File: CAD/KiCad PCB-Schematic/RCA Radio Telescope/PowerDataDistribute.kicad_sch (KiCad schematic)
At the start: 31 parts, among them J7 USB_A, J8 USB_A, Q1 DMP4047LFDE-7, U13 MIC23050-SYML-TR, U14 TPS62133RGTR

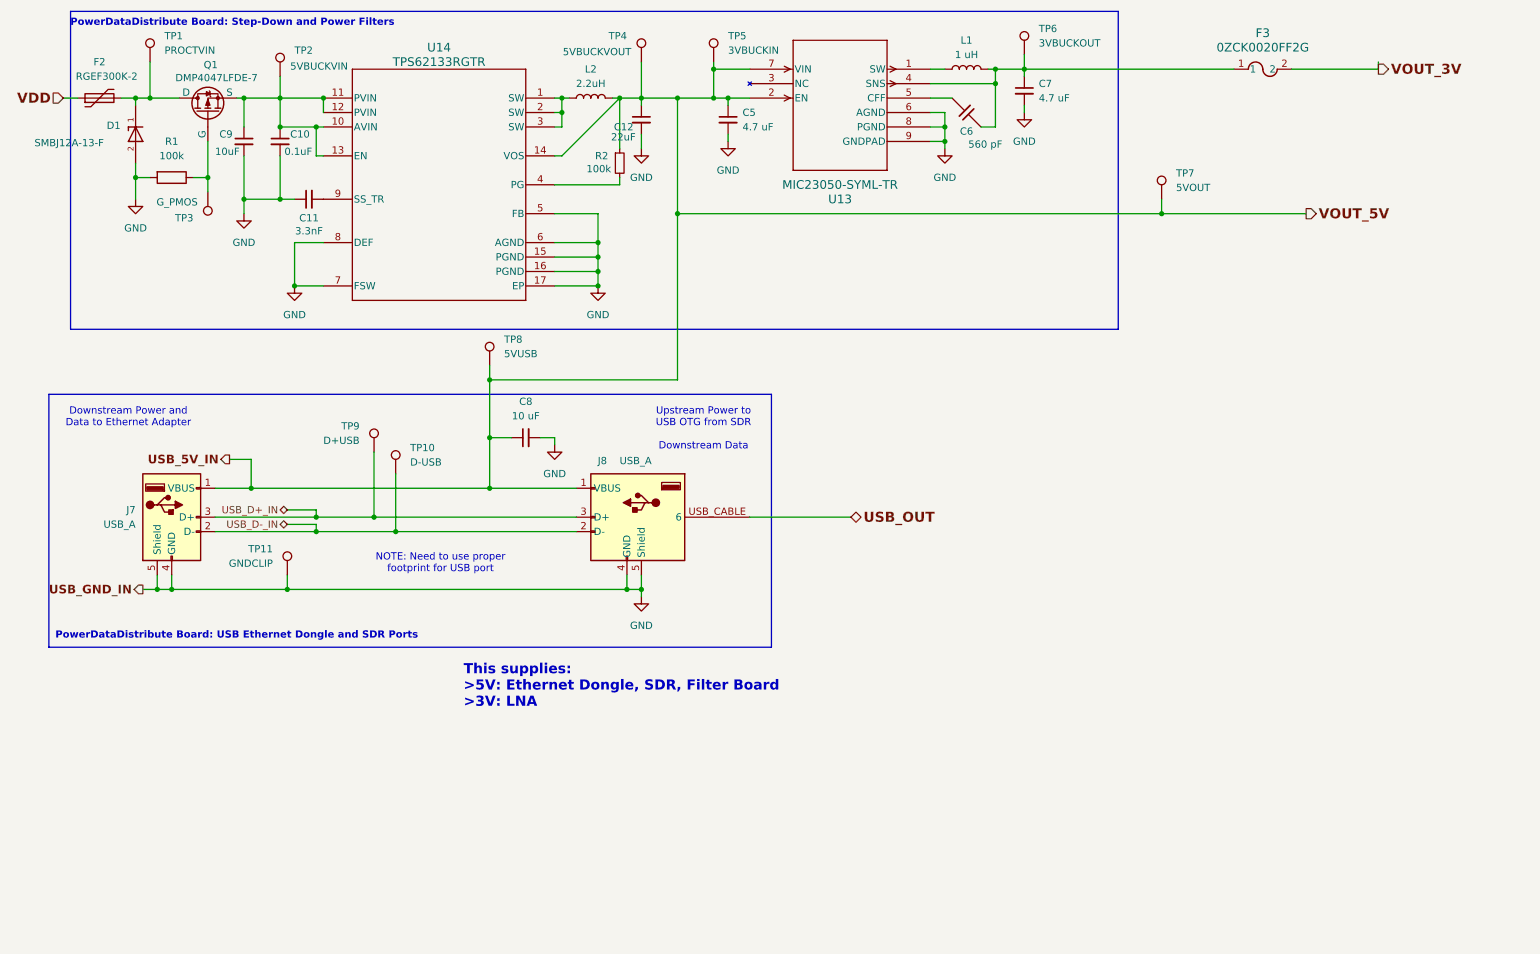
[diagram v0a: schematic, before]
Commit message: Updated PowerData Schematic to v1.8 and PCB to v1.7
- Swapped MIC Buck to LDO
- Changed footprint for Buck Inductor to appropriate component
- Rearranged PCB layout to accommodate new inductor
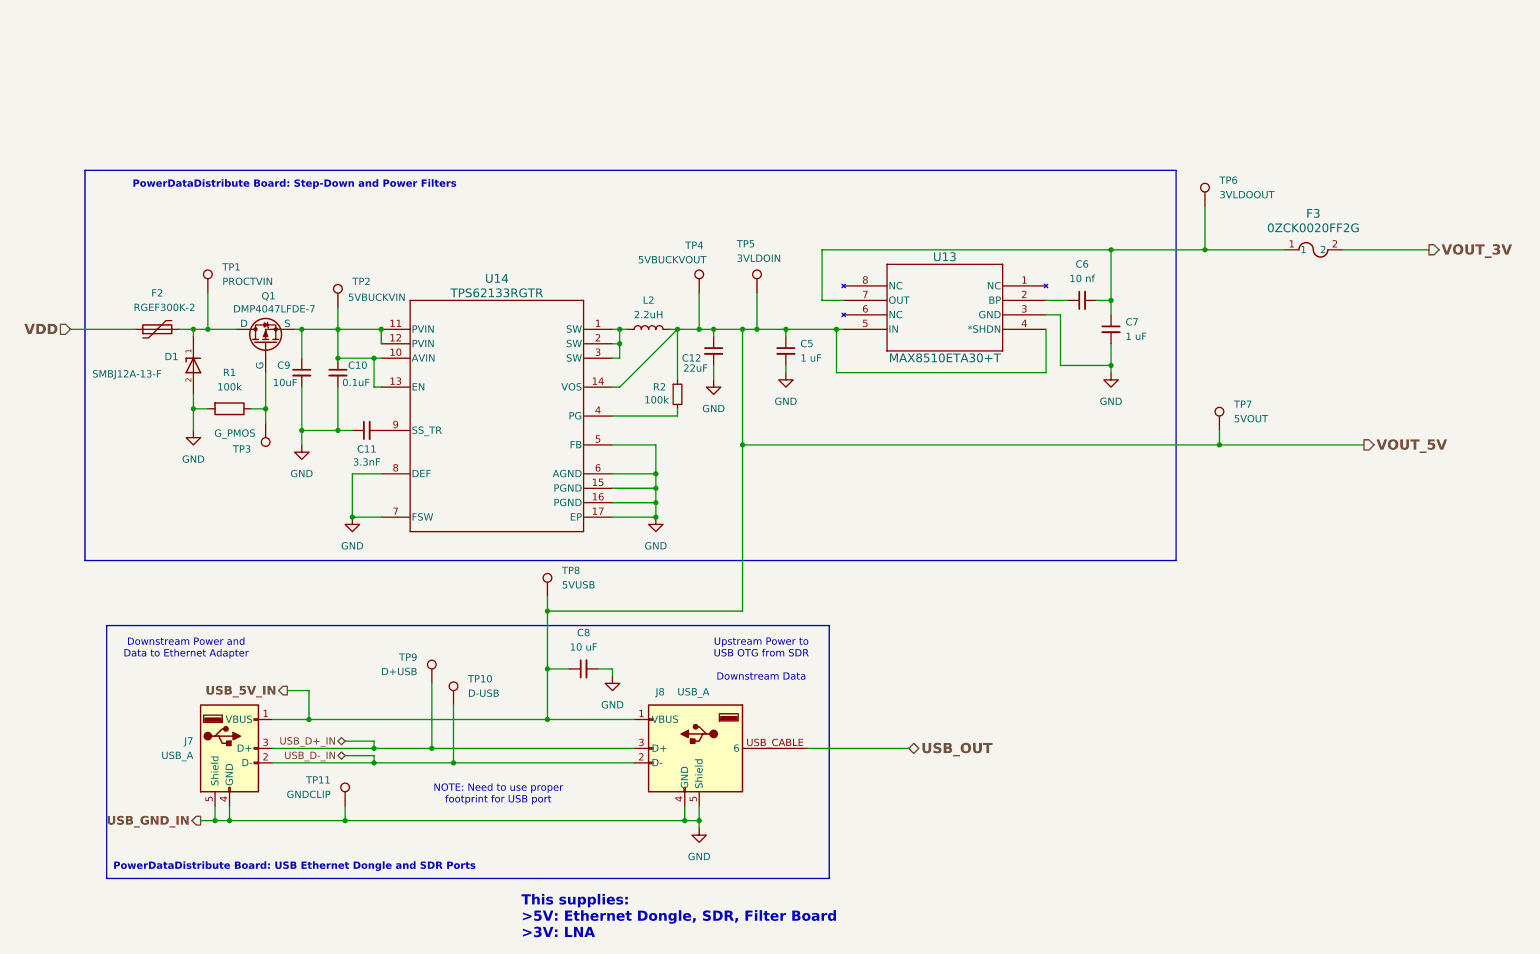
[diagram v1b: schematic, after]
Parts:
- removed C6: 560 pF, Capacitor_SMD:C_0805_2012Metric, symbol Device:C_45deg
- removed L1: 1 uH, Inductor_SMD:L_0805_2012Metric, symbol Device:L
- removed U13: MIC23050-SYML-TR, Library:MLF-8_ML_MCH, symbol Radio Telescope:MIC23050-SYML-TR
- added C6: 10 nf, Capacitor_SMD:C_0805_2012Metric, symbol Device:C_Small
- added U13: MAX8510ETA30+T, Library:21-0168E_T822-1_MXM, symbol Radio Telescope:MAX8510ETA30+T
- C5, C7: value 4.7 uF -> 1 uF
- L2: footprint Inductor_SMD:L_0805_2012Metric -> Library:IND_CB_DRA73
- TP5: value 3VBUCKIN -> 3VLDOIN
- TP6: value 3VBUCKOUT -> 3VLDOOUT
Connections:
- net GND: now also U13.3 (GND)
- net USB_5V_IN: now also U13.4 (*SHDN), U13.5 (IN)
- net at C7.1, F3.1, TP6.1: now also C6.2, U13.7 (OUT)
- new net: C6.1, U13.2 (BP)
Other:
- moved on the sheet: C10, C11, C12, C5, C7, C8, C9, D1, F2, F3, J7, J8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

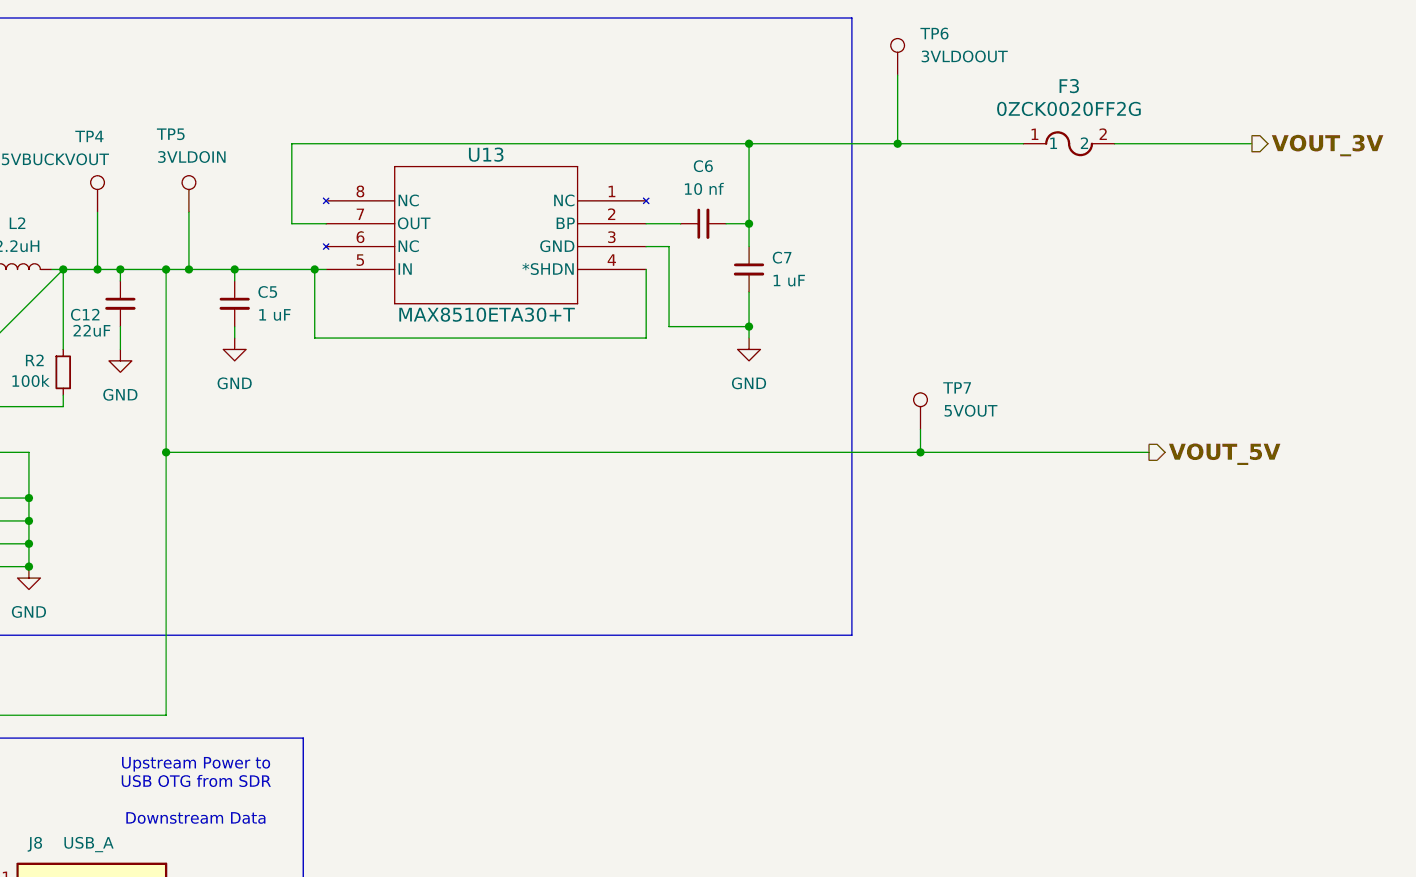
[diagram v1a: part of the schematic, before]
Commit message: Updated PowerData Schematic to v1.9 and PCB to v1.8
- Swapped LDO (Obsolete) with an Active version in both Schematic and PCB
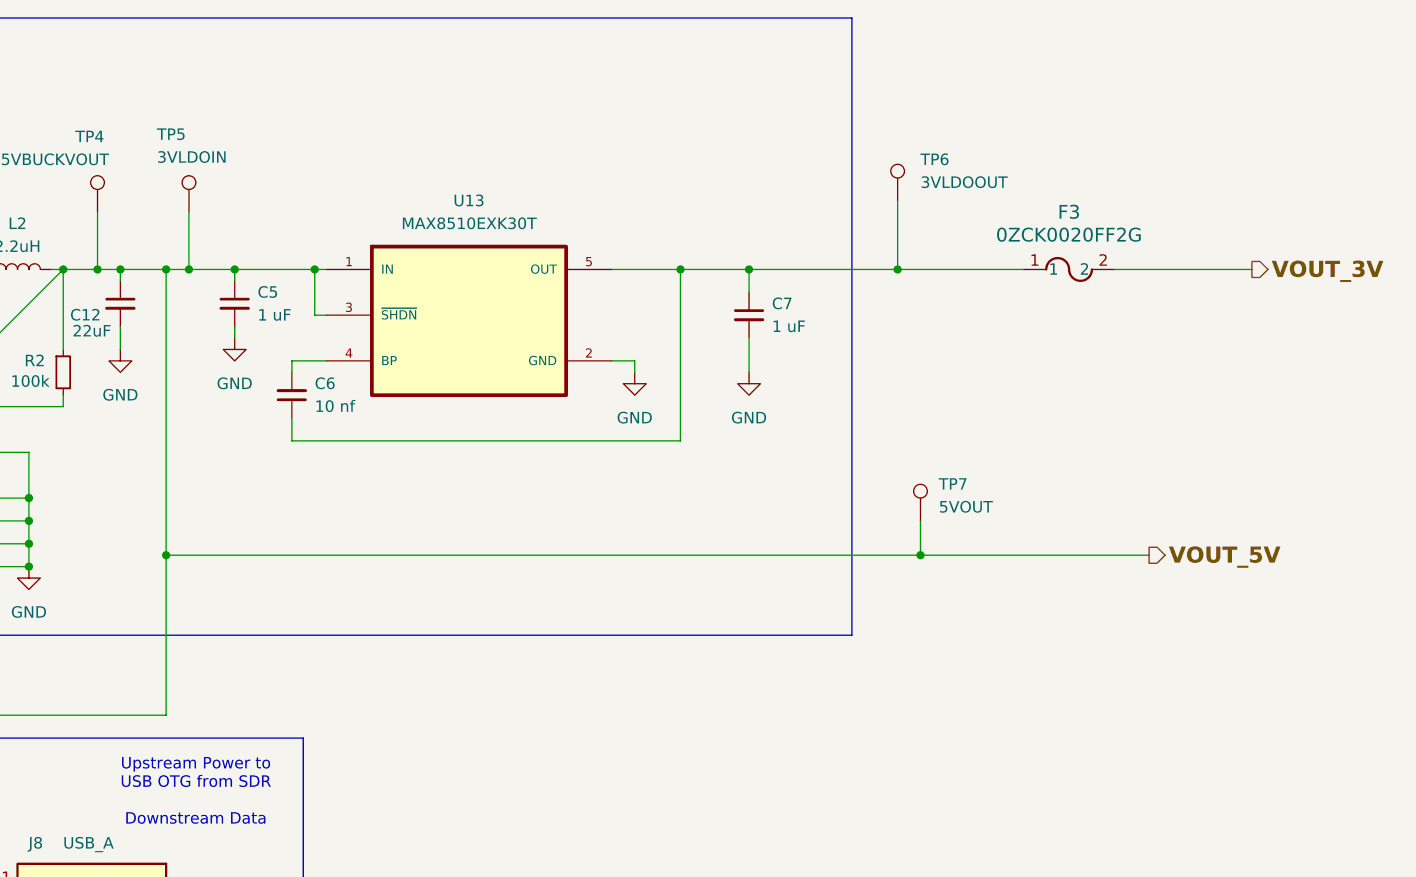
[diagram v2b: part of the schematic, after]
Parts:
- removed U13: MAX8510ETA30+T, Library:21-0168E_T822-1_MXM, symbol Radio Telescope:MAX8510ETA30+T
- added U13: MAX8510EXK30T, Library:SOT65P210X110-5N, symbol Radio Telescope:MAX8510EXK30T
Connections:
- net GND: now also U13.2 (GND)
- net USB_5V_IN: now also U13.1 (IN), U13.3 (~{SHDN})
- net at C6.1: now also C7.1, F3.1, TP6.1, U13.5 (OUT)
- new net: C6.2, U13.4 (BP)
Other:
- moved on the sheet: C6, C7, F3, TP6, TP7

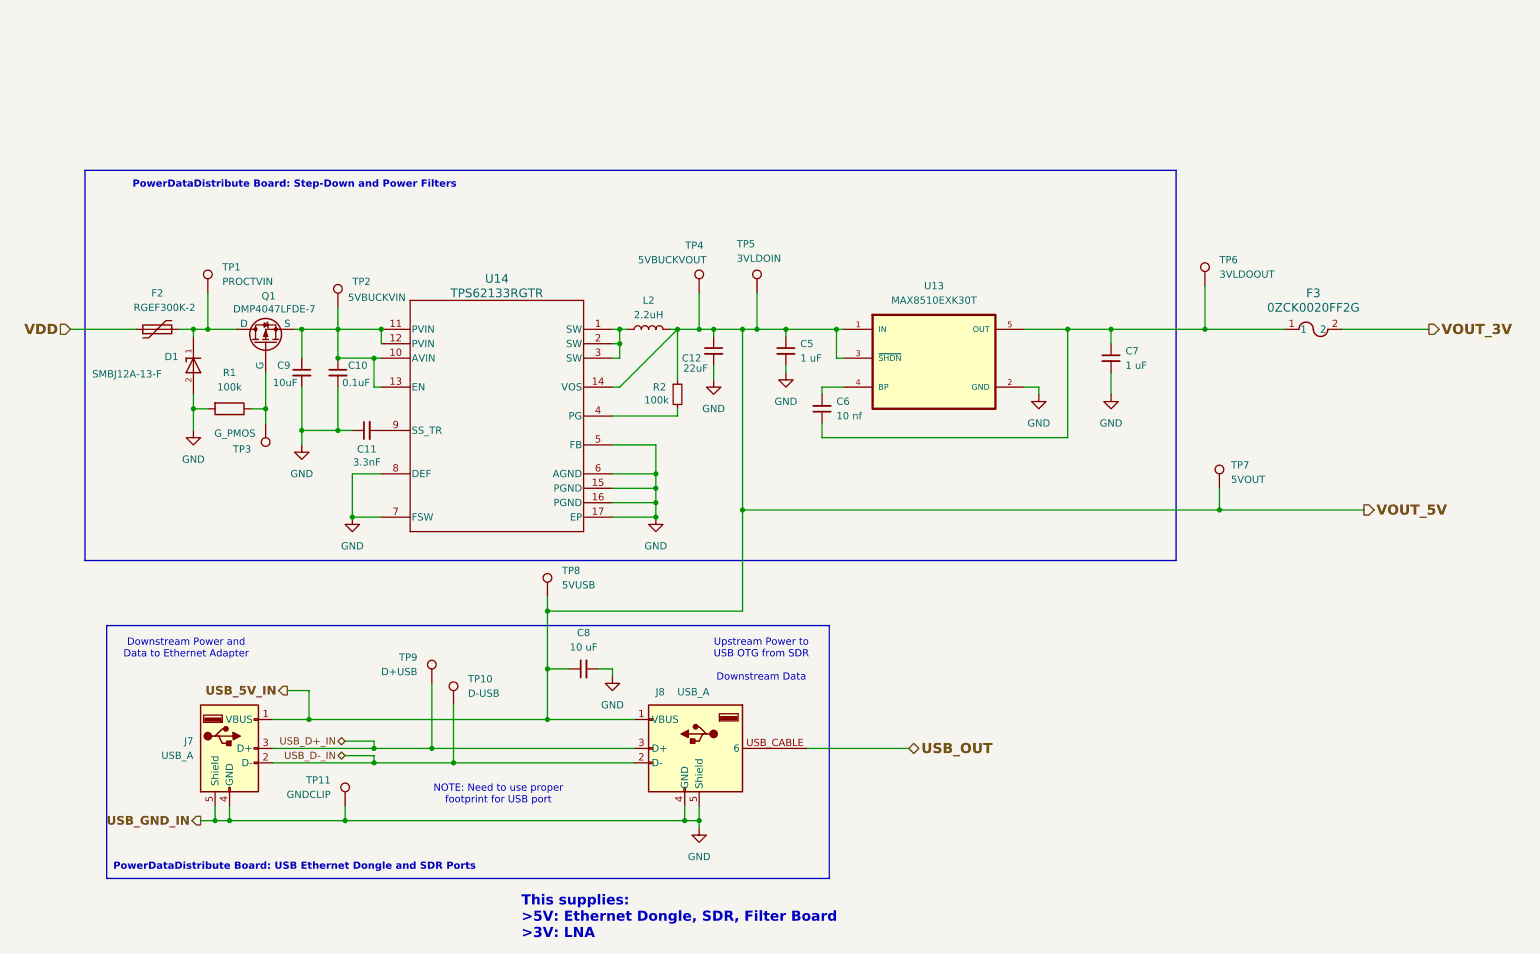
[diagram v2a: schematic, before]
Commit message: Updated PowerData Schematic to v2.0 and PCB to v1.9
- Added 0 Ohm resistors to modularized PCB
- Adjusted some GND vias to prevent clipping of silkscreen
- Edited LDO footprint to adhere with JLC specs
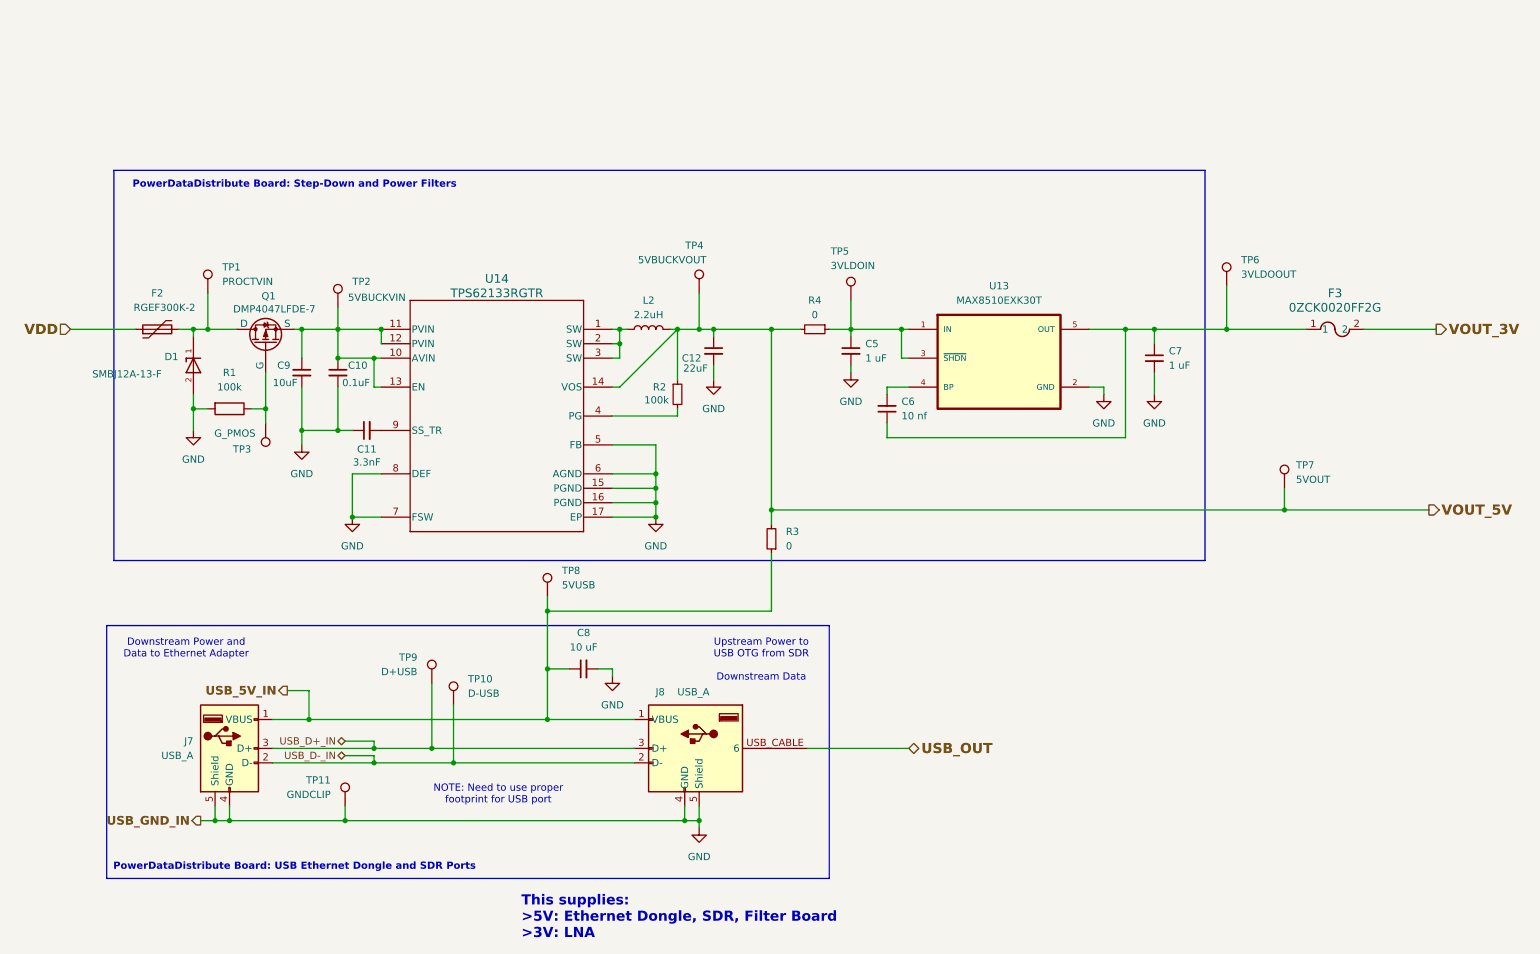
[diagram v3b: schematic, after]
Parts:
- added R3, R4: 0, Resistor_SMD:R_0805_2012Metric, symbol Device:R_Small
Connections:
- net USB_5V_IN: now also R3.1; no longer C12.1, C5.1, L2.2, R2.1, TP4.1, TP5.1, TP7.1, U13.1 (IN), U13.3 (~{SHDN}), U14.14 (VOS)
- new net: C5.1, R4.1, TP5.1, U13.1 (IN), U13.3 (~{SHDN})
- new net VOUT_5V: C12.1, L2.2, R2.1, R3.2, R4.2, TP4.1, TP7.1, U14.14 (VOS)
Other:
- moved on the sheet: C5, C6, C7, F3, TP5, TP6, TP7, U13

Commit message: Updated PowerData PCB to v2.1
- Added custom JLC rules from https://github.com/Cimos/KiCad-CustomDesignRules/tree/main
- Adjusted silkscreen according to new rules
- Added step models for components
- Adjusted via locations to be more spread out
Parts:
- TP1, TP10, TP2, TP3, TP4, TP5, TP6, TP7, TP8, TP9: footprint TestPoint:TestPoint_Pad_D1.0mm -> Library:TestPoint_Pad_D1.0mm_Edit
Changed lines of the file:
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@@
 			)
 		)
-		(property "Footprint" "TestPoint:TestPoint_Pad_D1.0mm"
+		(property "Footprint" "Library:TestPoint_Pad_D1.0mm_Edit"
 			(at 50.8 87.63 0)
 			(effects
@@
 			)
 		)
-		(property "Footprint" "TestPoint:TestPoint_Pad_D1.0mm"
+		(property "Footprint" "Library:TestPoint_Pad_D1.0mm_Edit"
 			(at 80.01 133.35 0)
 			(effects
@@
 			)
 		)
-		(property "Footprint" "TestPoint:TestPoint_Pad_D1.0mm"
+		(property "Footprint" "Library:TestPoint_Pad_D1.0mm_Edit"
 			(at 163.83 66.04 0)
 			(effects
@@
 			)
 		)
-		(property "Footprint" "TestPoint:TestPoint_Pad_D1.0mm"
+		(property "Footprint" "Library:TestPoint_Pad_D1.0mm_Edit"
 			(at 229.87 63.5 0)
 			(effects
@@
 			)
 		)
-		(property "Datasheet" "TPS62133RGTR"
+		(property "Datasheet" "https://www.ti.com/lit/ds/symlink/tps62130.pdf?HQS=dis-dk-null-digikeymode-dsf-pf-null-wwe&ts=1743207300295"
 			(at 96.52 86.36 0)
 			(effects
@@
 			)
 		)
-		(property "Footprint" "TestPoint:TestPoint_Pad_D1.0mm"
+		(property "Footprint" "Library:TestPoint_Pad_D1.0mm_Edit"
 			(at 73.66 67.31 0)
 			(effects
@@
 			)
 		)
-		(property "Footprint" "TestPoint:TestPoint_Pad_D1.0mm"
+		(property "Footprint" "Library:TestPoint_Pad_D1.0mm_Edit"
 			(at 110.49 118.11 0)
 			(effects
@@
 			)
 		)
-		(property "Footprint" "TestPoint:TestPoint_Pad_D1.0mm"
+		(property "Footprint" "Library:TestPoint_Pad_D1.0mm_Edit"
 			(at 127 64.77 0)
 			(effects
@@
 			)
 		)
-		(property "Footprint" "TestPoint:TestPoint_Pad_D1.0mm"
+		(property "Footprint" "Library:TestPoint_Pad_D1.0mm_Edit"
 			(at 93.98 137.16 0)
 			(effects
@@
 			)
 		)
-		(property "Footprint" "TestPoint:TestPoint_Pad_D1.0mm"
+		(property "Footprint" "Library:TestPoint_Pad_D1.0mm_Edit"
 			(at 50.8 64.77 0)
 			(effects
@@
 			)
 		)
-		(property "Footprint" "TestPoint:TestPoint_Pad_D1.0mm"
+		(property "Footprint" "Library:TestPoint_Pad_D1.0mm_Edit"
 			(at 240.03 99.06 0)
 			(effects
